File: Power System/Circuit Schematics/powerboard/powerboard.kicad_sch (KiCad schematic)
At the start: 14 parts, among them J1 Raspberry_Pi_2_3, J2 RJ45_LED, J3 RJ45_LED, J4 RJ45_LED, J5 RJ45_LED, U1 Pico, U2 Pico

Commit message: powerboard fixes
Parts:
- added R3, R4, R5, R6, R7, R? (x5): (no value), symbol Device:R_US
- BT1: value Battery -> (none)
- D1, D2, D3: value 1N4007 -> (none); footprint Diode_THT:D_DO-41_SOD81_P10.16mm_Horizontal -> (none)
- J1: value Raspberry_Pi_2_3 -> (none); symbol powerboard-rescue:Raspberry_Pi_2_3-Connector -> Connector:Raspberry_Pi_2_3
- J2, J3, J4, J5: value RJ45_LED -> (none)
- J6: renamed from J?; value TB002-500-02BE -> (none); footprint TB00250002BE -> (none)
- R1, R2: value R_Small_US -> (none)
- U1, U2: value Pico -> (none); footprint RPi_Pico:RPi_Pico_SMD_TH -> (none)
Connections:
- net GND: now also R6.2, R7.2, R?.2, R?.2, R?.2, R?.2, R?.2
- new net: R3.2, R4.1
- new net: R4.2, R5.1
- new net: R5.2, R6.1
- new net +BATT: R3.1
- new net -BATT: R7.1, R?.1, R?.1, R?.1, R?.1, R?.1

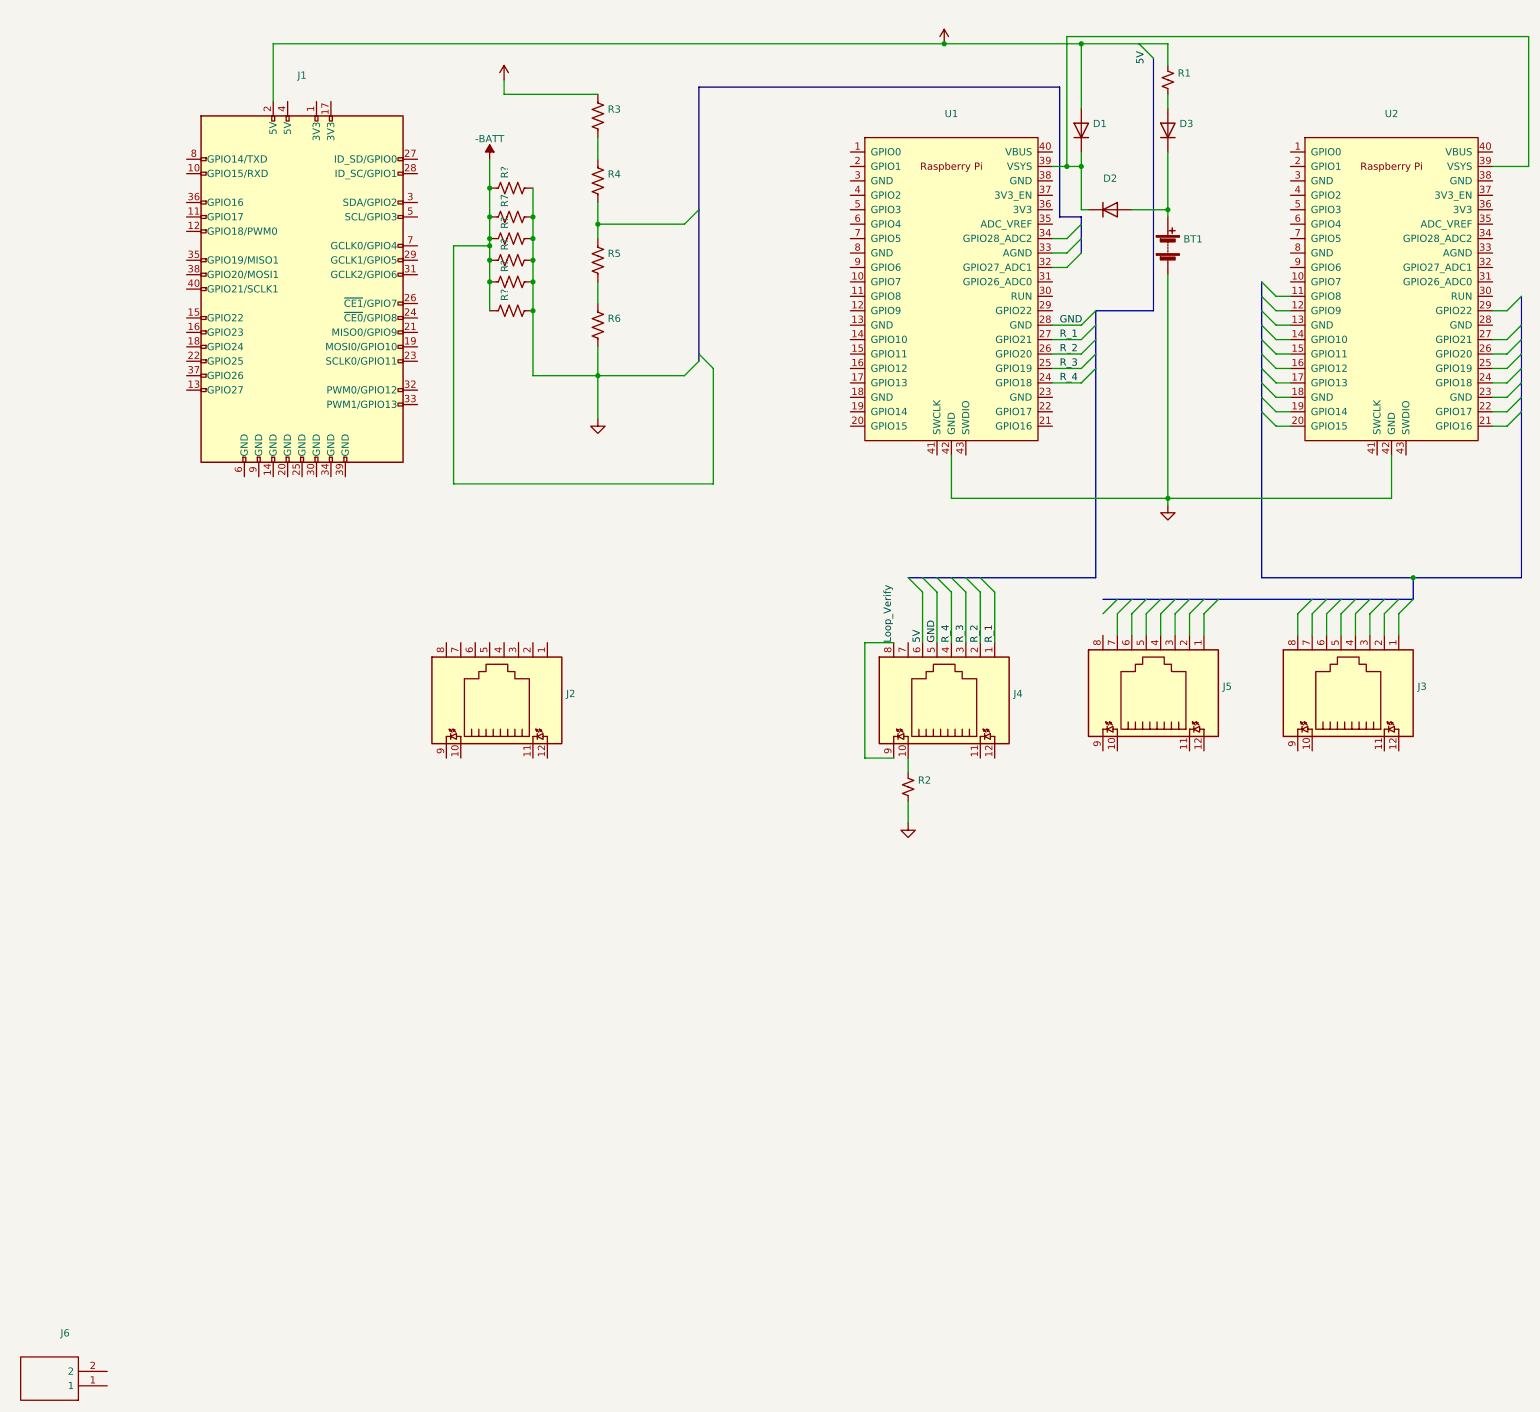
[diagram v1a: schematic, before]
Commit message: powerboard fixes
more powerboard fixes for file formatting
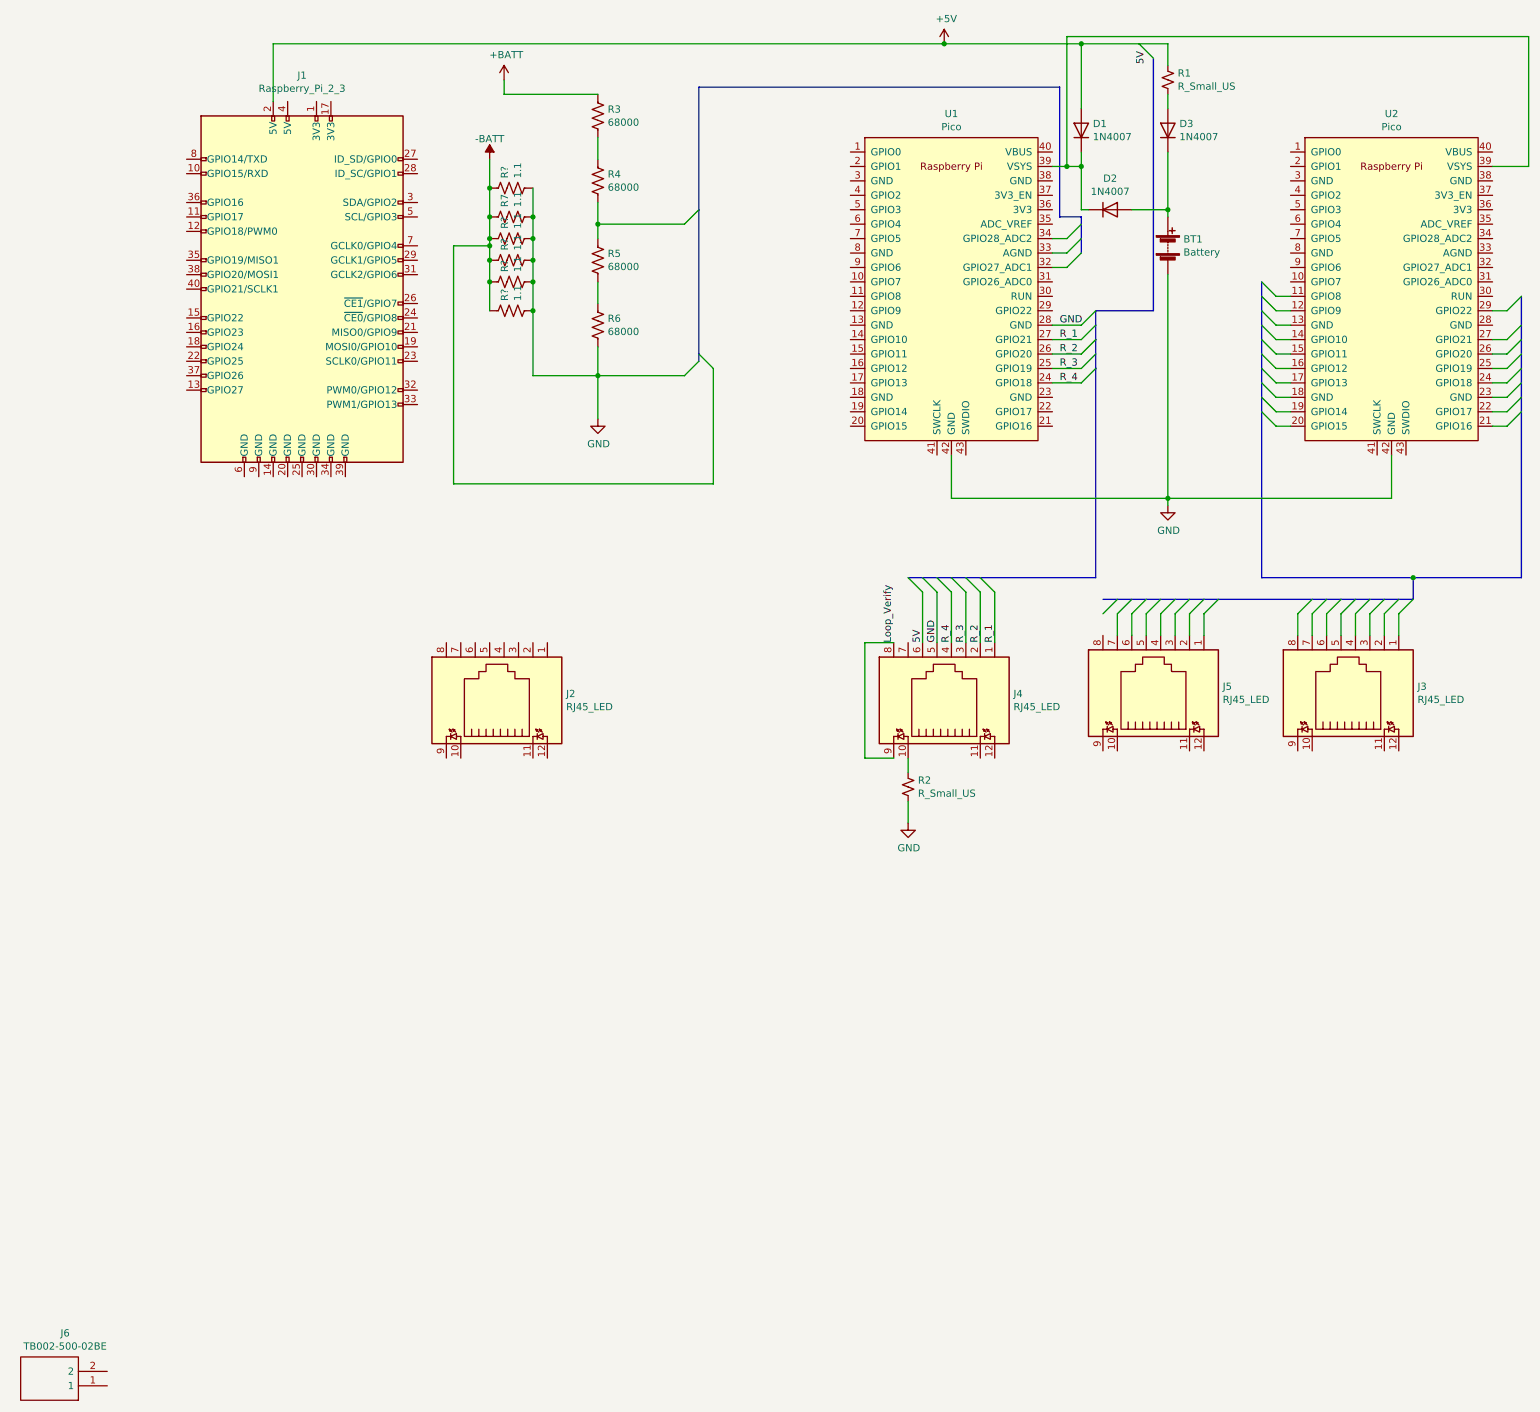
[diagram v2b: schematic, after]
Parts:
- BT1: value (none) -> Battery
- D1, D2, D3: value (none) -> 1N4007; footprint (none) -> Diode_THT:D_DO-41_SOD81_P10.16mm_Horizontal
- J1: value (none) -> Raspberry_Pi_2_3
- J2, J3, J4, J5: value (none) -> RJ45_LED
- J6: value (none) -> TB002-500-02BE; footprint (none) -> TB00250002BE
- R1, R2: value (none) -> R_Small_US
- R3, R4, R5, R6: value (none) -> 68000
- R7, R? (x5): value (none) -> 1.1
- U1, U2: value (none) -> Pico; footprint (none) -> RPi_Pico:RPi_Pico_SMD_TH
